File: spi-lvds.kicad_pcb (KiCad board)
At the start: 2 copper layers, 39.9 x 34.9 mm, 8 parts

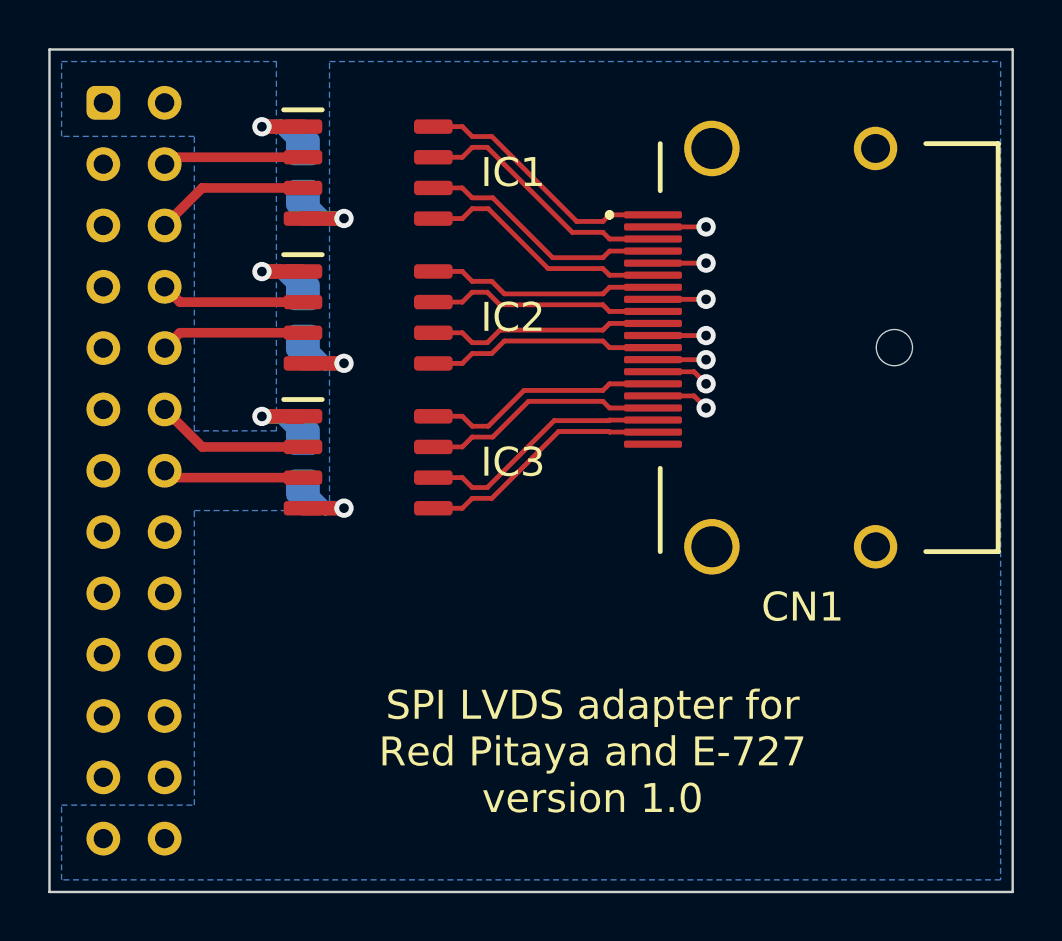
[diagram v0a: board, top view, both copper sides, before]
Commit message: improve filled zones
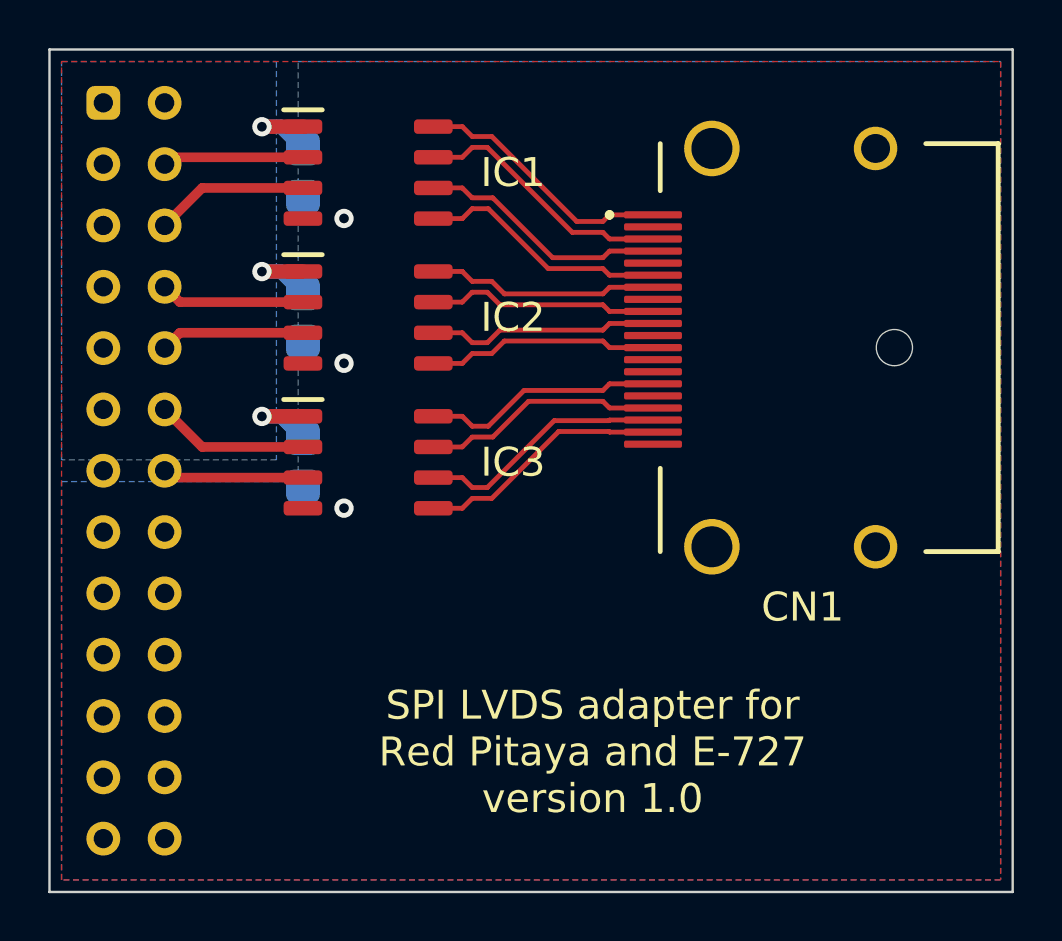
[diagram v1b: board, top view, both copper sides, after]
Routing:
- net GND: track 27.1 -> 0.02 mm, vias 10 -> 3
- added copper zone on F.Cu, net GND
